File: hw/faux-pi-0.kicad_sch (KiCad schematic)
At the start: 63 parts, among them J1 PWR_IN, J10 USB, J2 DEBUG, J3 RUN, J6 HDMI_C_1.4, J8 GPIO, J9 Micro_SD_Card_Det, SW1 RESET, SW2 BOOTSEL, U1 RP2040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

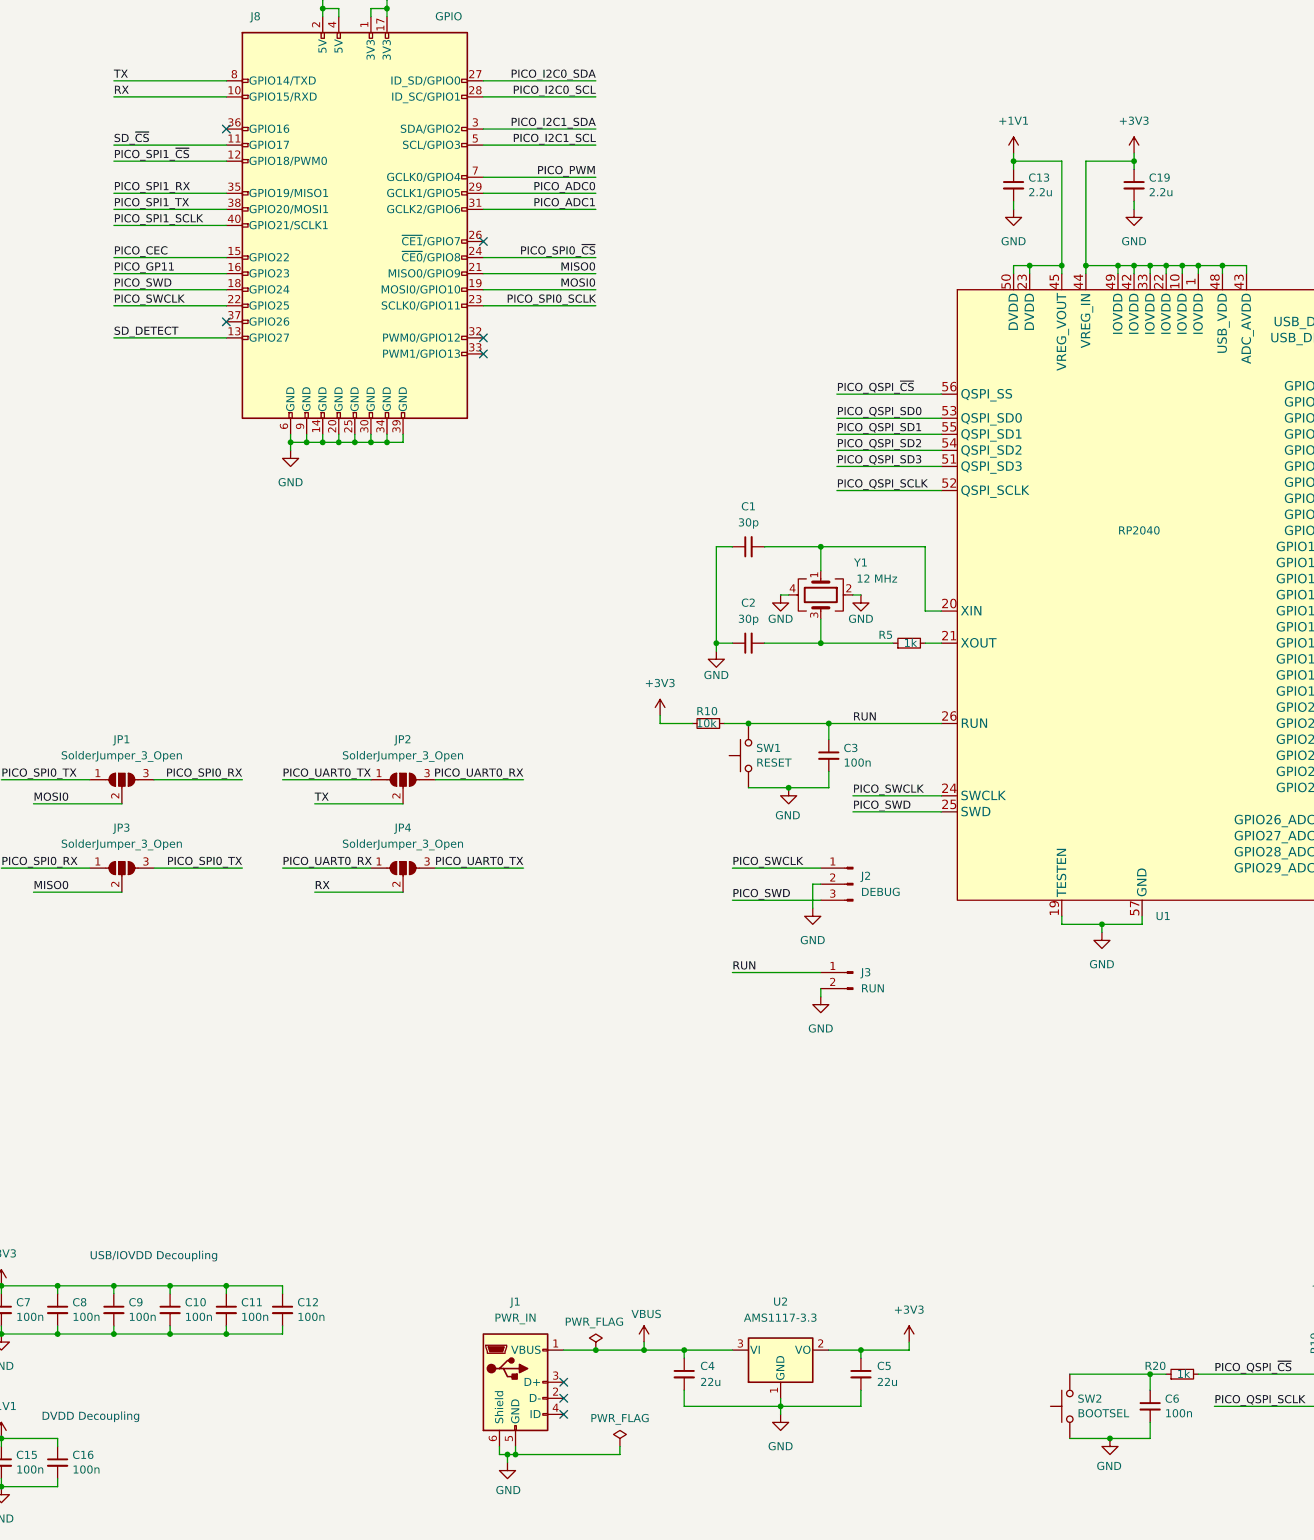
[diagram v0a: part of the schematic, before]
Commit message: Expose BOOTSEL and RUN on GPIO header
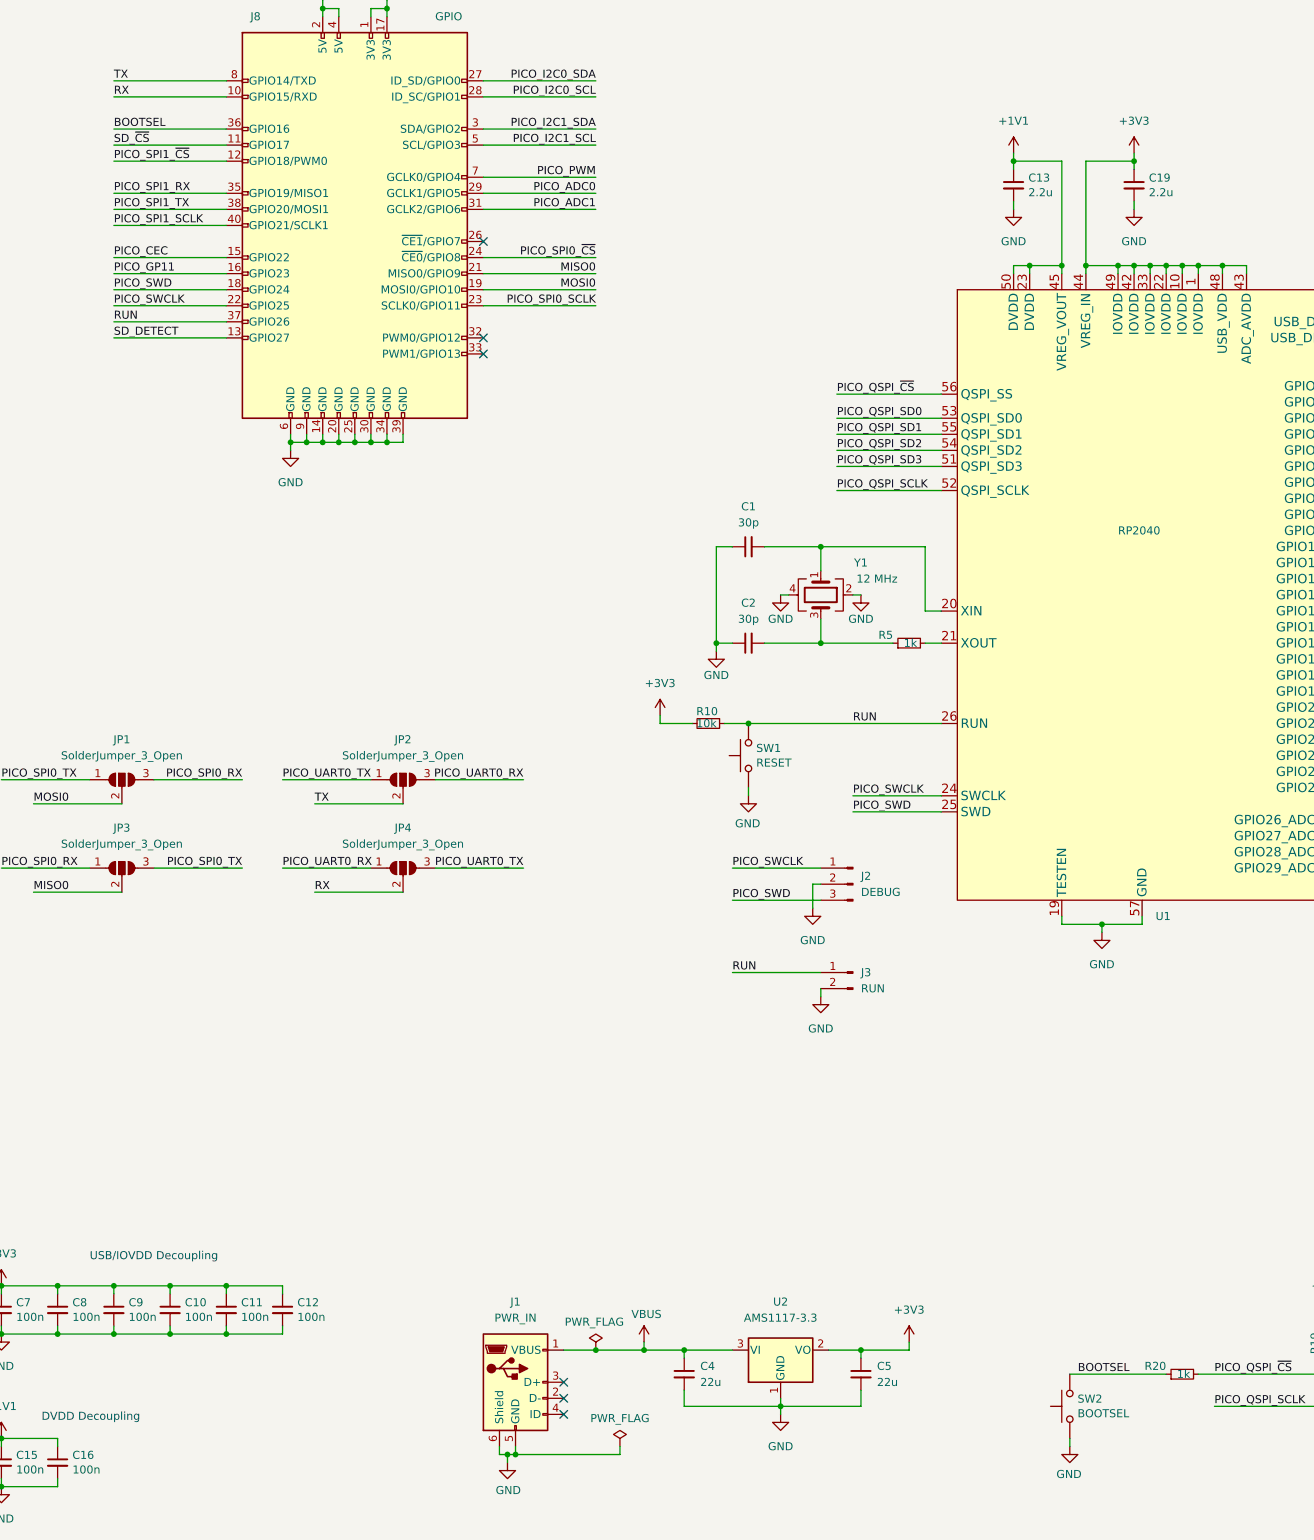
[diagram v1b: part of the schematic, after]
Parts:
- removed C3, C6: 100n, Capacitor_SMD:C_0402_1005Metric, symbol Device:C_Small
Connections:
- net RUN: now also J8.37 (GPIO26)
- net BOOTSEL: now reaches J8.36 (GPIO16)
- net BOOTSEL: now also R20.1, SW2.2
- no-connect marks 11 -> 9
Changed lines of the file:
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@@
   (junction (at 185.42 57.15) (diameter 0) (color 0 0 0 0)
   )
-  (junction (at 149.86 156.21) (diameter 0) (color 0 0 0 0)
-  )
   (junction (at 105.41 261.62) (diameter 0) (color 0 0 0 0)
   )
@@
   (junction (at 201.93 73.66) (diameter 0) (color 0 0 0 0)
   )
-  (junction (at 200.66 259.08) (diameter 0) (color 0 0 0 0)
-  )
   (junction (at 204.47 57.15) (diameter 0) (color 0 0 0 0)
   )
@@
   (junction (at 106.68 261.62) (diameter 0) (color 0 0 0 0)
   )
-  (junction (at 156.21 146.05) (diameter 0) (color 0 0 0 0)
-  )
   (junction (at 337.82 222.25) (diameter 0) (color 0 0 0 0)
   )
@@
   (junction (at 25.4 234.95) (diameter 0) (color 0 0 0 0)
   )
-  (junction (at 207.01 248.92) (diameter 0) (color 0 0 0 0)
-  )
   (junction (at 25.4 259.08) (diameter 0) (color 0 0 0 0)
   )
@@
   (no_connect (at 101.6 69.85))
   (no_connect (at 114.3 255.27))
-  (no_connect (at 60.96 82.55))
   (no_connect (at 372.11 135.89))
   (no_connect (at 372.11 133.35))
   (no_connect (at 342.9 53.34))
   (no_connect (at 114.3 252.73))
-  (no_connect (at 60.96 52.07))
   (no_connect (at 101.6 85.09))
   (no_connect (at 114.3 250.19))
@@
     (stroke (width 0) (type default) (color 0 0 0 0))
   )
-  (wire (pts (xy 156.21 146.05) (xy 173.99 146.05))
-    (stroke (width 0) (type default) (color 0 0 0 0))
-  )
   (wire (pts (xy 358.14 110.49) (xy 340.36 110.49))
     (stroke (width 0) (type default) (color 0 0 0 0))
@@
     (stroke (width 0) (type default) (color 0 0 0 0))
   )
-  (wire (pts (xy 207.01 251.46) (xy 207.01 248.92))
+  (wire (pts (xy 43.18 52.07) (xy 60.96 52.07))
     (stroke (width 0) (type default) (color 0 0 0 0))
   )
@@
     (stroke (width 0) (type default) (color 0 0 0 0))
   )
-  (wire (pts (xy 207.01 259.08) (xy 207.01 256.54))
-    (stroke (width 0) (type default) (color 0 0 0 0))
-  )
   (wire (pts (xy 204.47 55.88) (xy 204.47 57.15))
     (stroke (width 0) (type default) (color 0 0 0 0))
@@
     (stroke (width 0) (type default) (color 0 0 0 0))
   )
-  (wire (pts (xy 207.01 248.92) (xy 209.55 248.92))
+  (wire (pts (xy 194.31 248.92) (xy 209.55 248.92))
     (stroke (width 0) (type default) (color 0 0 0 0))
   )
@@
     (stroke (width 0) (type default) (color 0 0 0 0))
   )
-  (wire (pts (xy 143.51 146.05) (xy 156.21 146.05))
+  (wire (pts (xy 143.51 146.05) (xy 173.99 146.05))
     (stroke (width 0) (type default) (color 0 0 0 0))
   )
@@
     (stroke (width 0) (type default) (color 0 0 0 0))
   )
-  (wire (pts (xy 194.31 248.92) (xy 207.01 248.92))
-    (stroke (width 0) (type default) (color 0 0 0 0))
-  )
   (wire (pts (xy 43.18 241.3) (xy 43.18 242.57))
     (stroke (width 0) (type default) (color 0 0 0 0))
@@
     (stroke (width 0) (type default) (color 0 0 0 0))
   )
-  (wire (pts (xy 156.21 156.21) (xy 156.21 153.67))
-    (stroke (width 0) (type default) (color 0 0 0 0))
-  )
   (wire (pts (xy 384.81 146.05) (xy 384.81 147.32))
     (stroke (width 0) (type default) (color 0 0 0 0))
@@
     (stroke (width 0) (type default) (color 0 0 0 0))
   )
-  (wire (pts (xy 143.51 156.21) (xy 149.86 156.21))
+  (wire (pts (xy 143.51 156.21) (xy 143.51 157.48))
     (stroke (width 0) (type default) (color 0 0 0 0))
   )
@@
     (stroke (width 0) (type default) (color 0 0 0 0))
   )
-  (wire (pts (xy 149.86 156.21) (xy 156.21 156.21))
-    (stroke (width 0) (type default) (color 0 0 0 0))
-  )
   (wire (pts (xy 273.05 205.74) (xy 331.47 205.74))
     (stroke (width 0) (type default) (color 0 0 0 0))
@@
     (stroke (width 0) (type default) (color 0 0 0 0))
   )
+  (wire (pts (xy 43.18 82.55) (xy 60.96 82.55))
+    (stroke (width 0) (type default) (color 0 0 0 0))
+  )
   (wire (pts (xy 43.18 77.47) (xy 60.96 77.47))
     (stroke (width 0) (type default) (color 0 0 0 0))
@@
     (stroke (width 0) (type default) (color 0 0 0 0))
   )
-  (wire (pts (xy 194.31 259.08) (xy 200.66 259.08))
+  (wire (pts (xy 194.31 259.08) (xy 194.31 260.35))
     (stroke (width 0) (type default) (color 0 0 0 0))
   )
@@
     (stroke (width 0) (type default) (color 0 0 0 0))
   )
-  (wire (pts (xy 200.66 259.08) (xy 207.01 259.08))
-    (stroke (width 0) (type default) (color 0 0 0 0))
-  )
   (wire (pts (xy 237.49 153.67) (xy 255.27 153.67))
     (stroke (width 0) (type default) (color 0 0 0 0))
@@
     (stroke (width 0) (type default) (color 0 0 0 0))
   )
-  (wire (pts (xy 156.21 148.59) (xy 156.21 146.05))
-    (stroke (width 0) (type default) (color 0 0 0 0))
-  )
   (wire (pts (xy 345.44 175.26) (xy 345.44 173.99))
     (stroke (width 0) (type default) (color 0 0 0 0))
@@
     (effects (font (size 1.27 1.27)) (justify left bottom))
   )
+  (label "RUN" (at 43.18 82.55 0)
+    (effects (font (size 1.27 1.27)) (justify left bottom))
+  )
   (label "PICO_CEC" (at 43.18 72.39 0)
     (effects (font (size 1.27 1.27)) (justify left bottom))
@@
     (effects (font (size 1.27 1.27)) (justify right bottom))
   )
+  (label "BOOTSEL" (at 43.18 52.07 0)
+    (effects (font (size 1.27 1.27)) (justify left bottom))
+  )
   (label "SD_DETECT" (at 43.18 85.09 0)
     (effects (font (size 1.27 1.27)) (justify left bottom))
@@
     (effects (font (size 1.27 1.27)) (justify left bottom))
   )
+  (label "BOOTSEL" (at 195.58 248.92 0)
+    (effects (font (size 1.27 1.27)) (justify left bottom))
+  )
   (label "PICO_SPI0_SCLK" (at 255.27 107.95 180)
     (effects (font (size 1.27 1.27)) (justify right bottom))
@@
     (pin "1")
   )
-  (symbol (lib_id "Device:C_Small") (at 156.21 151.13 0) (unit 1)
-    (in_bom yes) (on_board yes)
-    (property "Reference" "C3" (id 0) (at 158.5468 149.9616 0)
-      (effects (font (size 1.27 1.27)) (justify left))
-    )
-    (property "Value" "100n" (id 1) (at 158.5468 152.273 0)
-      (effects (font (size 1.27 1.27)) (justify left))
-    )
-    (property "Footprint" "Capacitor_SMD:C_0402_1005Metric" (id 2) (at 156.21 151.13 0)
-      (effects (font (size 1.27 1.27)) hide)
-    )
-    (property "Datasheet" "~" (id 3) (at 156.21 151.13 0)
-      (effects (font (size 1.27 1.27)) hide)
-    )
-    (property "LCSC" "C1525" (id 4) (at 156.21 151.13 0)
-      (effects (font (size 1.27 1.27)) hide)
-    )
-    (pin "1")
-    (pin "2")
-  )
   (symbol (lib_id "Device:R_Small") (at 295.91 186.69 180) (unit 1)
     (in_bom yes) (on_board yes)
@@
     (pin "2")
   )
-  (symbol (lib_id "Device:C_Small") (at 207.01 254 0) (unit 1)
-    (in_bom yes) (on_board yes)
-    (property "Reference" "C6" (id 0) (at 209.3468 252.8316 0)
-      (effects (font (size 1.27 1.27)) (justify left))
-    )
-    (property "Value" "100n" (id 1) (at 209.3468 255.143 0)
-      (effects (font (size 1.27 1.27)) (justify left))
-    )
-    (property "Footprint" "Capacitor_SMD:C_0402_1005Metric" (id 2) (at 207.01 254 0)
-      (effects (font (size 1.27 1.27)) hide)
-    )
-    (property "Datasheet" "~" (id 3) (at 207.01 254 0)
-      (effects (font (size 1.27 1.27)) hide)
-    )
-    (property "LCSC" "C1525" (id 4) (at 207.01 254 0)
-      (effects (font (size 1.27 1.27)) hide)
-    )
-    (pin "1")
-    (pin "2")
-  )
-  (symbol (lib_id "power:GND") (at 149.86 156.21 0) (mirror y) (unit 1)
+  (symbol (lib_id "power:GND") (at 143.51 157.48 0) (mirror y) (unit 1)
     (in_bom yes) (on_board yes)
-    (property "Reference" "#PWR0124" (id 0) (at 149.86 162.56 0)
+    (property "Reference" "#PWR0124" (id 0) (at 143.51 163.83 0)
       (effects (font (size 1.27 1.27)) hide)
     )
-    (property "Value" "GND" (id 1) (at 149.733 160.6042 0))
-    (property "Footprint" "" (id 2) (at 149.86 156.21 0)
+    (property "Value" "GND" (id 1) (at 143.383 161.8742 0))
+    (property "Footprint" "" (id 2) (at 143.51 157.48 0)
       (effects (font (size 1.27 1.27)) hide)
     )
-    (property "Datasheet" "" (id 3) (at 149.86 156.21 0)
+    (property "Datasheet" "" (id 3) (at 143.51 157.48 0)
       (effects (font (size 1.27 1.27)) hide)
     )
@@
     (pin "2")
   )
-  (symbol (lib_id "power:GND") (at 200.66 259.08 0) (mirror y) (unit 1)
+  (symbol (lib_id "power:GND") (at 194.31 260.35 0) (mirror y) (unit 1)
     (in_bom yes) (on_board yes)
-    (property "Reference" "#PWR0114" (id 0) (at 200.66 265.43 0)
+    (property "Reference" "#PWR0114" (id 0) (at 194.31 266.7 0)
       (effects (font (size 1.27 1.27)) hide)
     )
-    (property "Value" "GND" (id 1) (at 200.533 263.4742 0))
-    (property "Footprint" "" (id 2) (at 200.66 259.08 0)
+    (property "Value" "GND" (id 1) (at 194.183 264.7442 0))
+    (property "Footprint" "" (id 2) (at 194.31 260.35 0)
       (effects (font (size 1.27 1.27)) hide)
     )
-    (property "Datasheet" "" (id 3) (at 200.66 259.08 0)
+    (property "Datasheet" "" (id 3) (at 194.31 260.35 0)
       (effects (font (size 1.27 1.27)) hide)
     )
@@
       (reference "C2") (unit 1) (value "30p") (footprint "Capacitor_SMD:C_0402_1005Metric")
     )
-    (path "/34e97286-2ba5-464c-a15b-904e1234823e"
-      (reference "C3") (unit 1) (value "100n") (footprint "Capacitor_SMD:C_0402_1005Metric")
-    )
     (path "/d6fa2dc3-e193-41b4-81db-8551f2d85c79"
       (reference "C4") (unit 1) (value "22u") (footprint "Capacitor_SMD:C_0805_2012Metric")
@@
       (reference "C5") (unit 1) (value "22u") (footprint "Capacitor_SMD:C_0805_2012Metric")
     )
-    (path "/6a741a99-41e0-45fa-a80f-9d4ff8c93b44"
-      (reference "C6") (unit 1) (value "100n") (footprint "Capacitor_SMD:C_0402_1005Metric")
-    )
     (path "/23c66706-ce2f-479a-9e57-7e78082697e0"

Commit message: docs & remove UART jumpers
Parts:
- removed JP2, JP4: SolderJumper_3_Open, Jumper:SolderJumper-3_P1.3mm_Open_RoundedPad1.0x1.5mm, symbol Jumper:SolderJumper_3_Open
- JP1: value SolderJumper_3_Open -> SPI0_PICO
- JP3: value SolderJumper_3_Open -> SPI0_POCI
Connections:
- net RX is gone; now on net PICO_UART0_RX: J8.10 (GPIO15/RXD)
- net TX is gone; now on net PICO_UART0_TX: J8.8 (GPIO14/TXD)
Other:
- note added: "DANGER: Closing DVI_SCL and DVI_SDA enabels 5V pullups on pins 27 and 28 of the GPIO header. Only do this if you know what you're doing!"
- note added: "DVI Display"
- note added: "Flash"
- note added: "GPIO"
- note added: "Micro SD"
- note added: "Power"
- note added: "SPI0 Role"
- note added: "These jumpers swap SPI0 TX/RX to select between controller and peripheral roles."
- note added: "USB"
- title: (none) -> Faux Pi Zero
- moved on the sheet: C1, C10, C11, C12, C13, C14, C15, C16, C17, C18, C19, C2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
